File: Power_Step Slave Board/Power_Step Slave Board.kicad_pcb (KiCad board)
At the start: 2 copper layers, 69.4 x 49.1 mm, 23 parts, among them P1 CONN_01X04, P10 CONN_01X04, P11 CONN_01X02, P12 CONN_01X04, P13 CONN_01X04, P2 CONN_01X04, P3 CONN_01X02, P4 CONN_01X02, P5 CONN_01X04, P6 CONN_01X02, P7 CONN_01X04, P8 CONN_01X02, P9 CONN_01X04

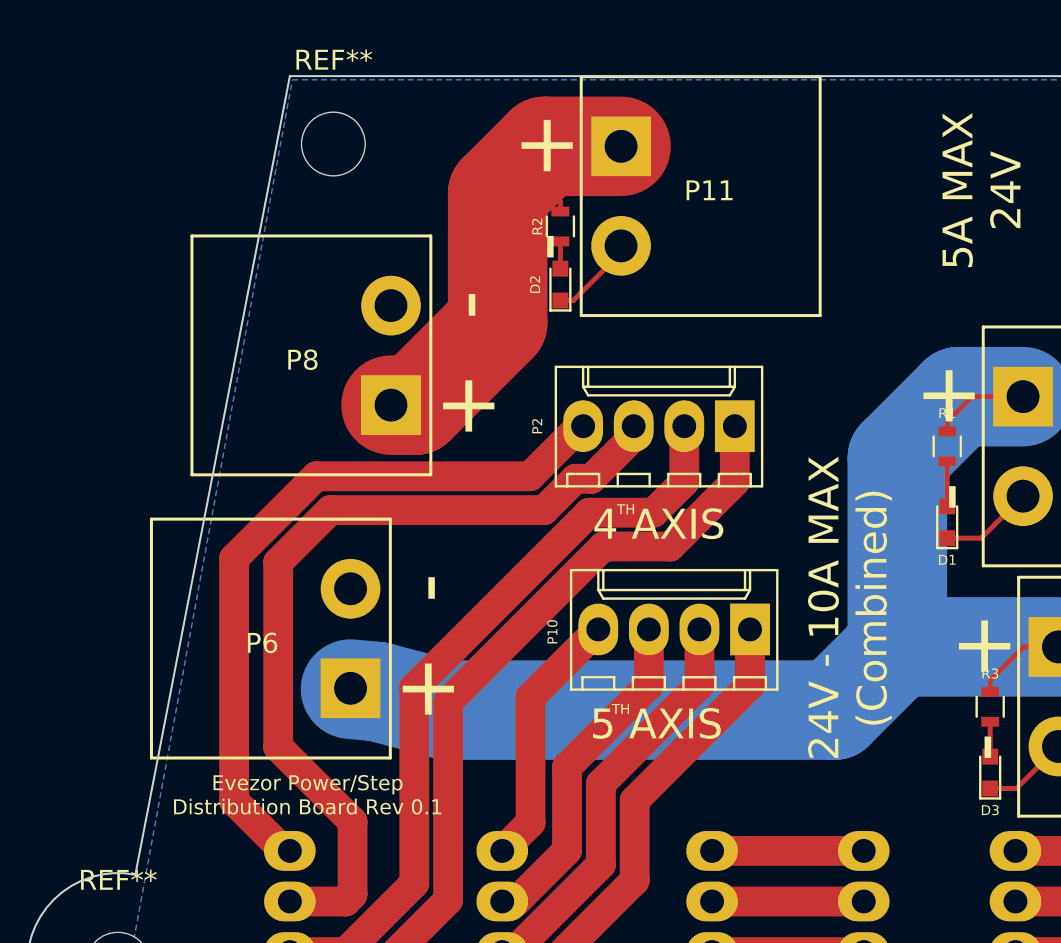
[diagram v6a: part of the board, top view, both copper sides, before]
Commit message: silkscreen additions
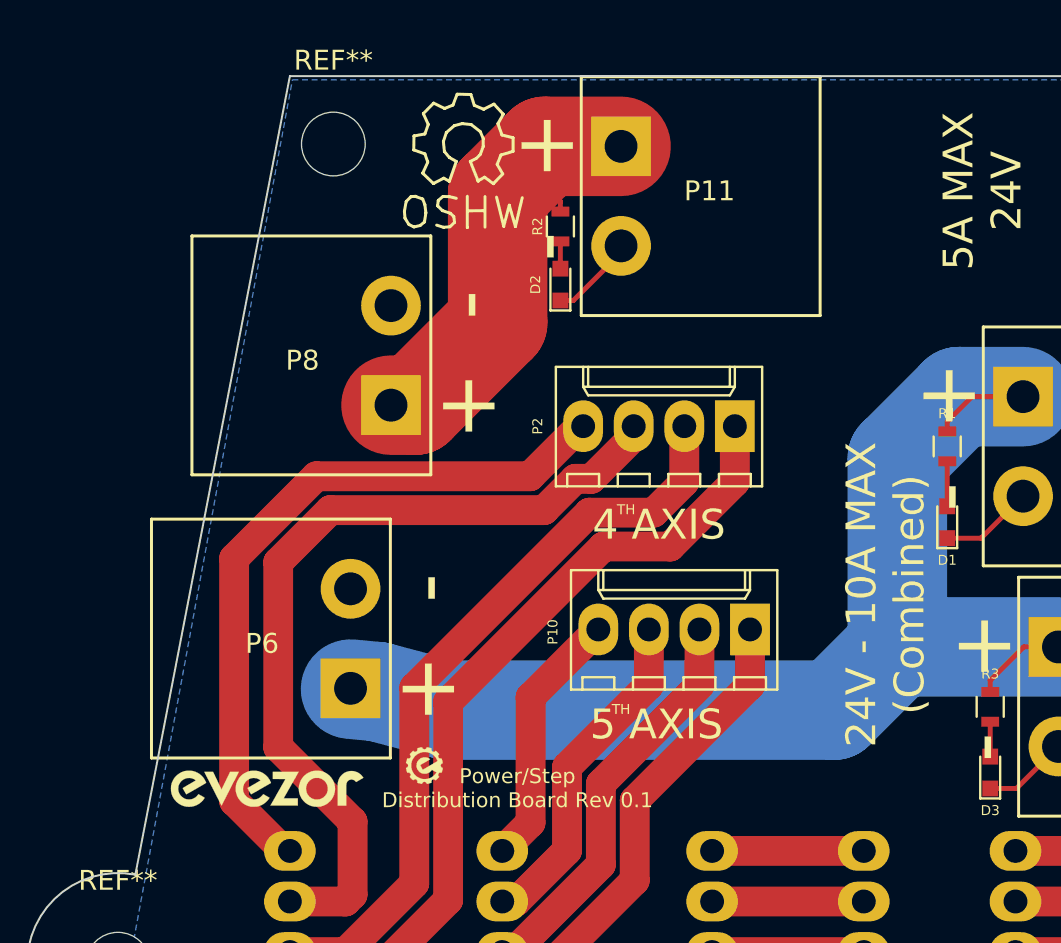
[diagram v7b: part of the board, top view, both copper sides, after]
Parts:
- added G***: LOGO, ASSETS:evezor_18, F.Cu at (125.9, 116.3)
- added G***: LOGO, ASSETS:GEAR_18, F.Cu at (133.8, 115.1)
- added REF**: Symbol_OSHW-Logo_SilkScreen, ASSETS:Symbol_OSHW-Logo_SilkScreen, F.Cu at (135.7, 83.8)
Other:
- board text added: "Power/Step Distribution Board Rev 0.1"
- board text removed: "Evezor Power/Step Distribution Board Rev 0.1"

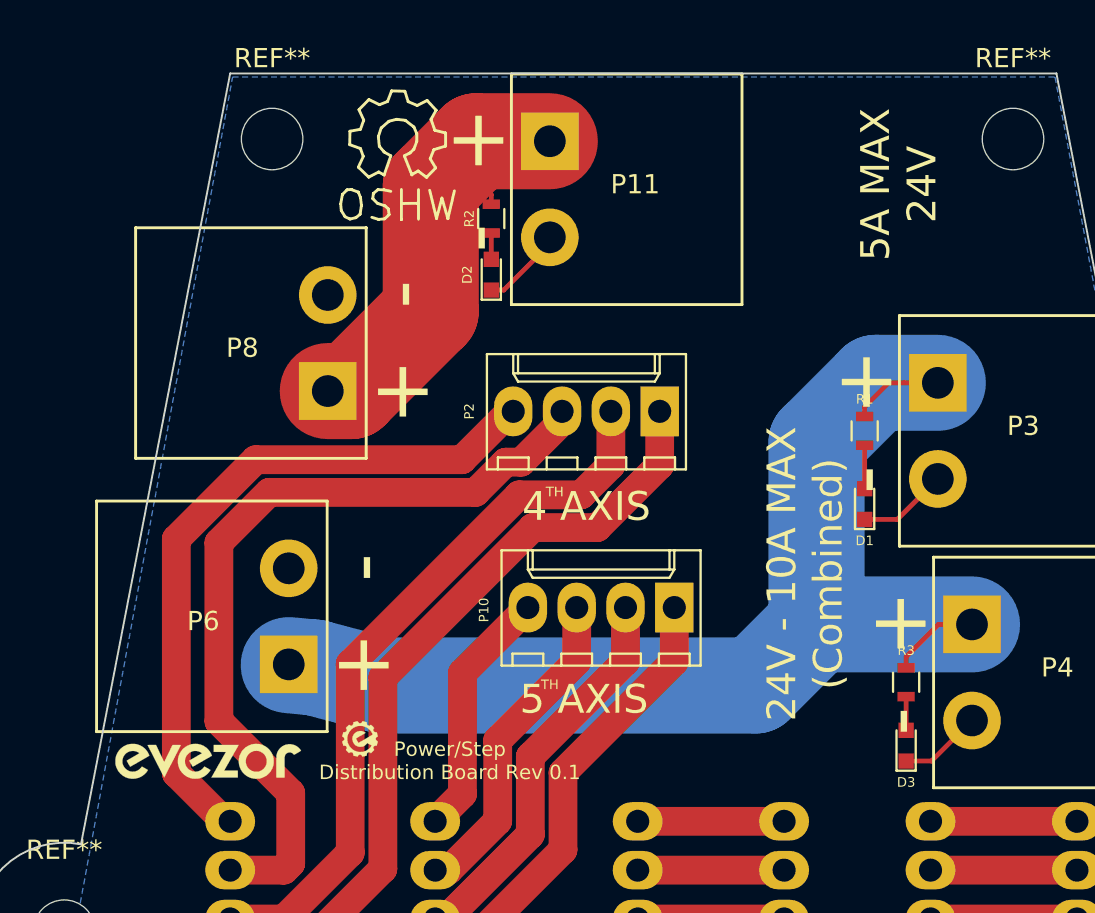
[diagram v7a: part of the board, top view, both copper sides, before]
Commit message: rotated 5A connector
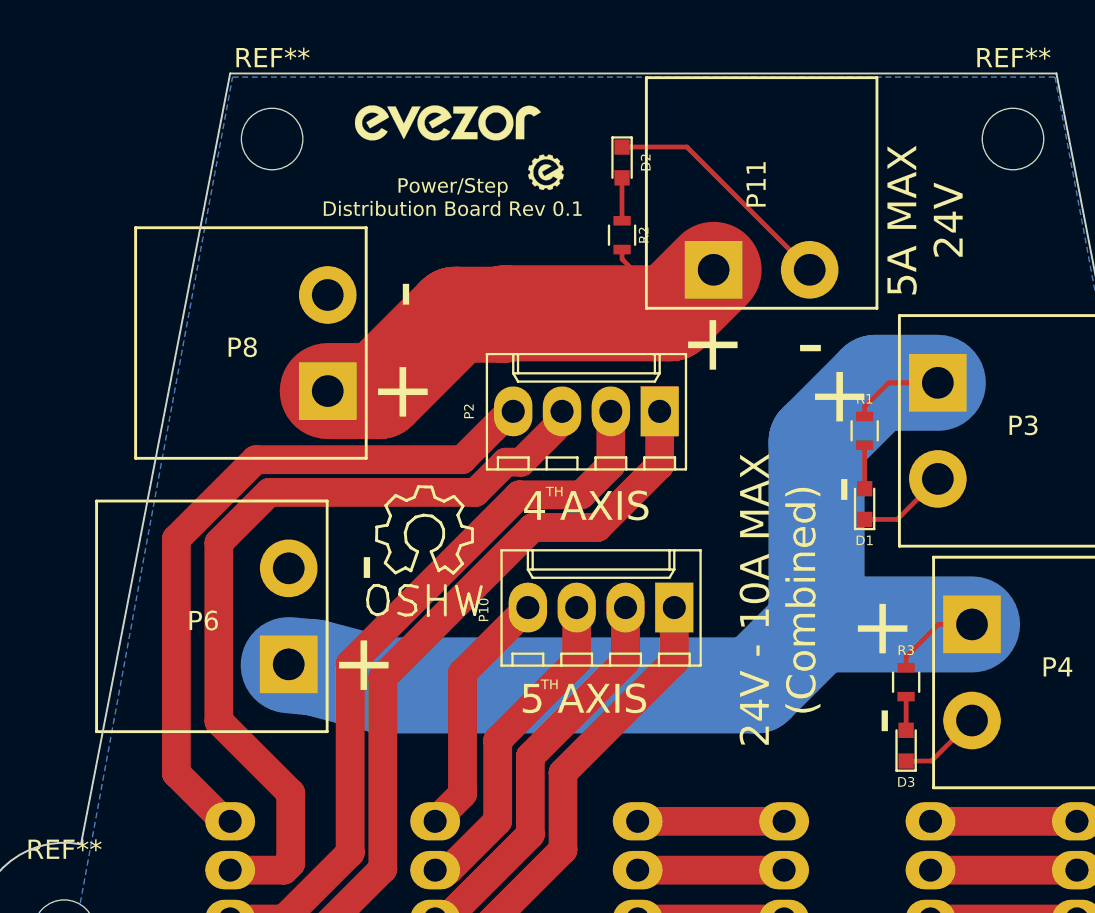
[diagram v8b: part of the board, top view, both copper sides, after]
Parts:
- moved G*** 35.5 mm to (138.3, 83.0)
- moved G*** 31.0 mm to (143.4, 85.6)
- moved REF** 20.6 mm to (137.1, 104.4)
- moved P11 11.8 mm to (154.7, 90.7), turned to 180 degrees
- moved D2 8.97 mm to (147.4, 85.1), turned to 270 degrees
- moved R2 6.86 mm to (147.4, 88.9), turned to 270 degrees
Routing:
- net Net-(P11-Pad2): track 24.6 -> 38.2 mm
- net GND: track 13.4 -> 21.4 mm
- net Net-(D2-Pad2): track 1.37 -> 2.23 mm
